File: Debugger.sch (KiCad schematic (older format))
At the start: 2 parts, among them P8 SERIAL, P9 POWER

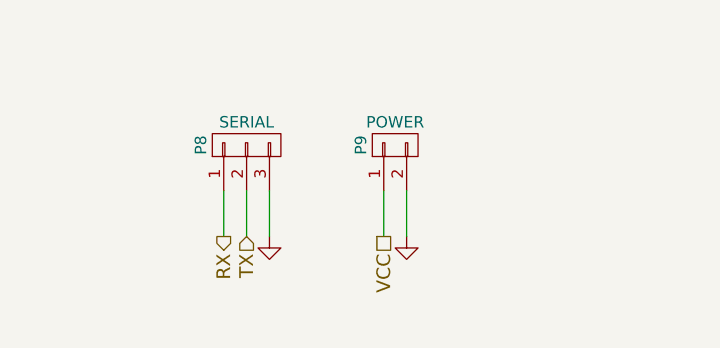
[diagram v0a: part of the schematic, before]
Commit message: Changes to be committed: 	new file:   78LXXSOT89.pdf 	modified:   Control.sch 	modified:   Debugger.sch 	modified:   MotorDriver.sch 	modified:   PS.sch 	modified:   Sensor.sch 	new file:   XL6009-Schematic-Diagram.pdf 	modified:   main-cache.lib 	new file:   main.cmp 	new file:   main.kicad_pcb 	new file:   main.net 	modified:   main.pro 	modified:   main.sch
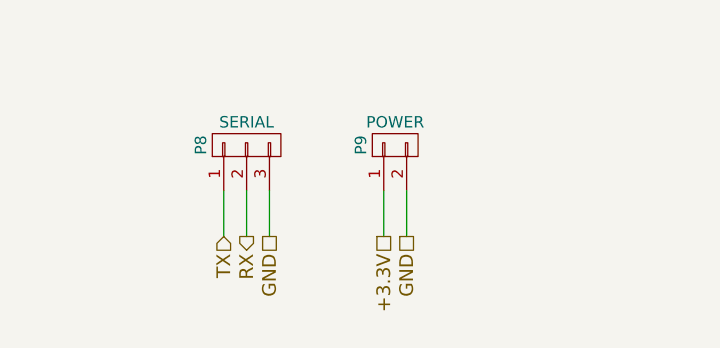
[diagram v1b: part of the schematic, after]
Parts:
- P8: footprint (none) -> Pin_Headers:Pin_Header_Straight_1x03
- P9: footprint (none) -> Pin_Headers:Pin_Header_Straight_1x02
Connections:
- net RX: now also P8.2 (P2); no longer P8.1 (P1)
- net TX: now also P8.1 (P1); no longer P8.2 (P2)
- net VCC renamed +3.3V
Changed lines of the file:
@@
 EESchema Schematic File Version 2
+LIBS:main-rescue
 LIBS:power
 LIBS:device
@@
 LIBS:contrib
 LIBS:main-cache
+LIBS:tcrt5000
 EELAYER 25 0
 EELAYER END
@@
 F 0 "P8" H 1650 3850 50  0000 C CNN
 F 1 "SERIAL" V 1750 3650 50  0000 C CNN
-F 2 "" H 1650 3650 60  0000 C CNN
+F 2 "Pin_Headers:Pin_Header_Straight_1x03" H 1650 3650 60  0001 C CNN
 F 3 "" H 1650 3650 60  0000 C CNN
 	1    1650 3650
@@
 F 0 "P9" H 2300 3800 50  0000 C CNN
 F 1 "POWER" V 2400 3650 50  0000 C CNN
-F 2 "" H 2300 3650 60  0000 C CNN
+F 2 "Pin_Headers:Pin_Header_Straight_1x02" H 2300 3650 60  0001 C CNN
 F 3 "" H 2300 3650 60  0000 C CNN
 	1    2300 3650
 	0    -1   -1   0
 $EndComp
-Text HLabel 1550 4050 3    60   Output ~ 0
+Text HLabel 1650 4050 3    60   Output ~ 0
 RX
-Text HLabel 1650 4050 3    60   Input ~ 0
+Text HLabel 1550 4050 3    60   Input ~ 0
 TX
-$Comp
-L GND #PWR014
-U 1 1 558DA613
-P 1750 4050
-F 0 "#PWR014" H 1750 4050 30  0001 C CNN
-F 1 "GND" H 1750 3980 30  0001 C CNN
-F 2 "" H 1750 4050 60  0000 C CNN
-F 3 "" H 1750 4050 60  0000 C CNN
-	1    1750 4050
-	1    0    0    -1
-$EndComp
-$Comp
-L GND #PWR015
-U 1 1 558DA627
-P 2350 4050
-F 0 "#PWR015" H 2350 4050 30  0001 C CNN
-F 1 "GND" H 2350 3980 30  0001 C CNN
-F 2 "" H 2350 4050 60  0000 C CNN
-F 3 "" H 2350 4050 60  0000 C CNN
-	1    2350 4050
-	1    0    0    -1
-$EndComp
 Wire Wire Line
 	2350 3850 2350 4050
@@
 	1550 3850 1550 4050
 Text HLabel 2250 4050 3    60   UnSpc ~ 0
-VCC
++3.3V
 Wire Wire Line
 	2250 3850 2250 4050
@@
 Text Notes 2200 2050 0    60   ~ 12
 AWAS 3.3V
+Text HLabel 2350 4050 3    60   UnSpc ~ 0
+GND
+Text HLabel 1750 4050 3    60   UnSpc ~ 0
+GND
 $EndSCHEMATC

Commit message: update
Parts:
- renumbered P9 to P10, P8 to P9
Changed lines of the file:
@@
 LIBS:memory
 LIBS:xilinx
-LIBS:special
 LIBS:microcontrollers
 LIBS:dsp
@@
 encoding utf-8
 Sheet 6 6
-Title ""
-Date ""
-Rev ""
+Title "KENZANIN LINEFOLLOWER"
+Date "2015-06-28"
+Rev "1.0"
 Comp ""
 Comment1 ""
@@
 https://www.bukalapak.com/p/elektronik/lain-lain-208/96p2m-jual-esp8266-esp11-esp-11-wifi-module-serial-wifi-for-arduino-minsys-dll?from=list-product
 $Comp
-L CONN_01X03 P8
+L CONN_01X03 P9
 U 1 1 558DA3D1
 P 1650 3650
-F 0 "P8" H 1650 3850 50  0000 C CNN
+F 0 "P9" H 1650 3850 50  0000 C CNN
 F 1 "SERIAL" V 1750 3650 50  0000 C CNN
 F 2 "Pin_Headers:Pin_Header_Straight_1x03" H 1650 3650 60  0001 C CNN
@@
 $EndComp
 $Comp
-L CONN_01X02 P9
+L CONN_01X02 P10
 U 1 1 558DA47F
 P 2300 3650
-F 0 "P9" H 2300 3800 50  0000 C CNN
+F 0 "P10" H 2300 3800 50  0000 C CNN
 F 1 "POWER" V 2400 3650 50  0000 C CNN
 F 2 "Pin_Headers:Pin_Header_Straight_1x02" H 2300 3650 60  0001 C CNN
@@
 65 32 A2 50 A1 F7 CC 9B AA E0 07 94 2A 24 E9 56 1E F9 2D CA 38 F0 66 C2 22 FA B3 F1 42 9F C8 F3
 E8 F7 BF C4 81 63 A2 94 56 3B 1F FA 38 66 32 E2 D3 27 AE AE F2 0B 7E 99 FE 0F F2 E8 67 06 73 94
-30 EC 00 00 00 00 49 45 4E 44 AE 42 60 82 00
+30 EC 00 00 00 00 49 45 4E 44 AE 42 60 82 B8
 EndData
 $EndBitmap
